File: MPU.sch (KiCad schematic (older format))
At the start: 32 parts, among them J1 MICRO-USB, P1 BL_PAD, P10 CONN_01X01, P11 CONN_01X04, P2 SWD_DAT, P3 SWD_CLK, P4 SWD_3V3, P5 SWD_GND, P6 SWD_RST, P8 CONN_01X01, P9 CONN_01X01, SW1 SW_PUSH, SW2 SW_PUSH, U4 SAMD21E17A, Y1 32.768kHz

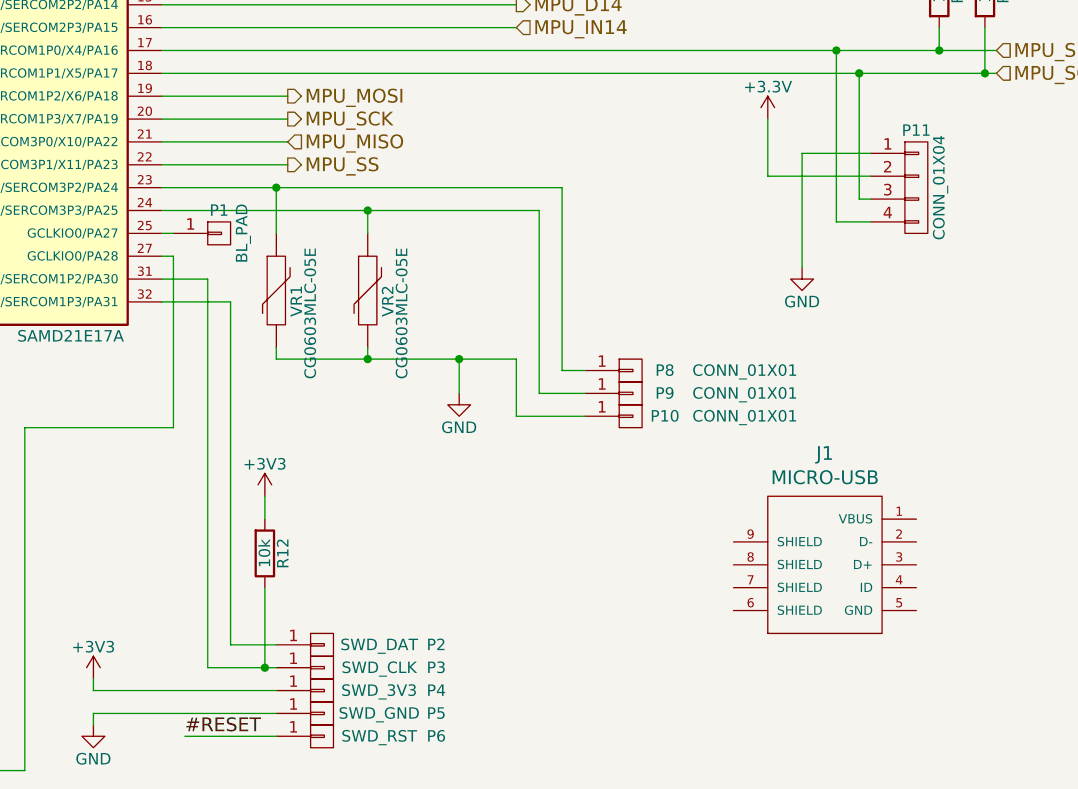
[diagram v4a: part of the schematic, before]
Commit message: Started work to add the power mux and USB connector
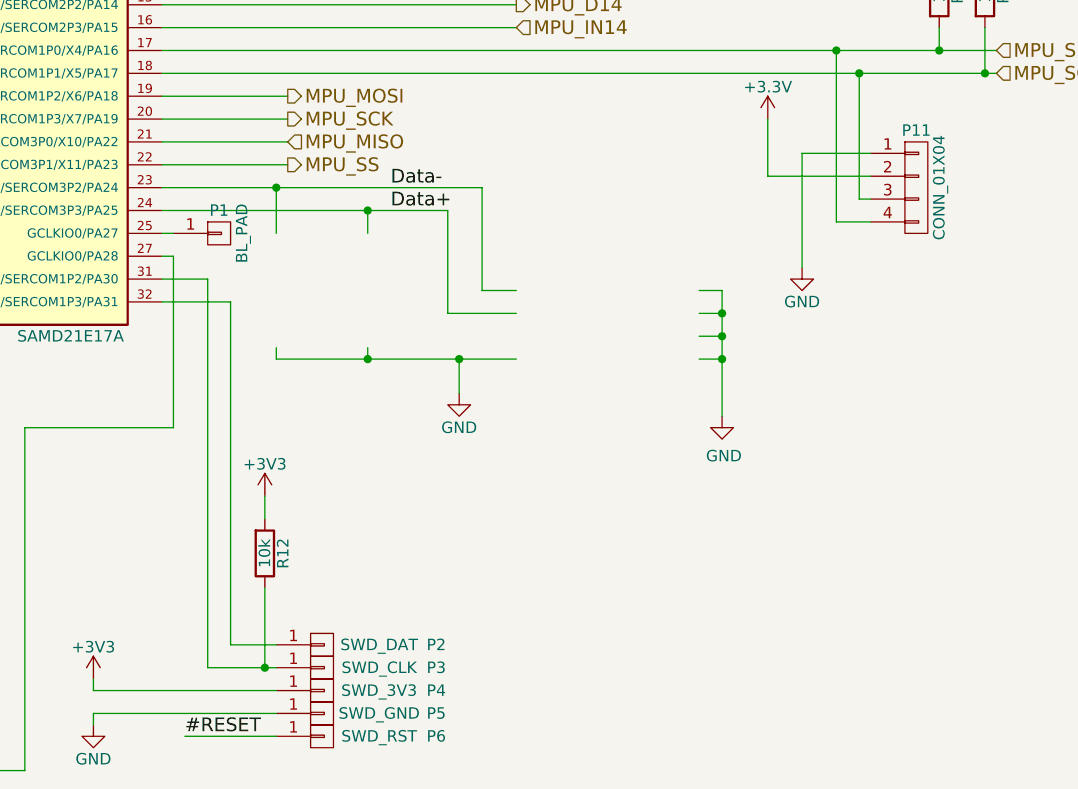
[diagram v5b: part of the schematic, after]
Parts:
- removed J1: MICRO-USB, RocketScreamKicadLibrary:MICRO-USB, symbol MICRO-USB
- removed P10, P8, P9: CONN_01X01, Measurement_Points:Measurement_Point_Round-TH_Small, symbol CONN_01X01
- removed VR1, VR2: CG0603MLC-05E, Capacitors_SMD:C_0603, symbol VR
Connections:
- net labels added: Data+, Data-
- wire segments 107 -> 110
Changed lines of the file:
@@
-	1    0    0    -1
-$EndComp
-$Comp
-L VR VR1
-U 1 1 56C25FED
-P 6150 4100
-F 0 "VR1" V 6210 4054 50  0000 C TNN
-F 1 "CG0603MLC-05E" V 6300 4000 50  0000 C CNN
-F 2 "Capacitors_SMD:C_0603" H 6150 4100 50  0001 C CNN
-F 3 "" H 6150 4100 50  0000 C CNN
-	1    6150 4100
-	1    0    0    -1
-$EndComp
-$Comp
-L VR VR2
-U 1 1 56C2603F
-P 6550 4100
-F 0 "VR2" V 6610 4054 50  0000 C TNN
-F 1 "CG0603MLC-05E" V 6700 4000 50  0000 C CNN
-F 2 "Capacitors_SMD:C_0603" H 6550 4100 50  0001 C CNN
-F 3 "" H 6550 4100 50  0000 C CNN
-	1    6550 4100
 	1    0    0    -1
 $EndComp
@@
 	1    0    0    -1
 $EndComp
-$Comp
-L CONN_01X01 P8
-U 1 1 56C3BE2F
-P 7700 4450
-F 0 "P8" H 7850 4450 50  0000 C CNN
-F 1 "CONN_01X01" H 8200 4450 50  0000 C CNN
-F 2 "Measurement_Points:Measurement_Point_Round-TH_Small" H 7700 4450 50  0001 C CNN
-F 3 "" H 7700 4450 50  0000 C CNN
-	1    7700 4450
-	1    0    0    -1
-$EndComp
-$Comp
-L CONN_01X01 P9
-U 1 1 56C3BE98
-P 7700 4550
-F 0 "P9" H 7850 4550 50  0000 C CNN
-F 1 "CONN_01X01" H 8200 4550 50  0000 C CNN
-F 2 "Measurement_Points:Measurement_Point_Round-TH_Small" H 7700 4550 50  0001 C CNN
-F 3 "" H 7700 4550 50  0000 C CNN
-	1    7700 4550
-	1    0    0    -1
-$EndComp
-$Comp
-L CONN_01X01 P10
-U 1 1 56C3BF04
-P 7700 4650
-F 0 "P10" H 7850 4650 50  0000 C CNN
-F 1 "CONN_01X01" H 8200 4650 50  0000 C CNN
-F 2 "Measurement_Points:Measurement_Point_Round-TH_Small" H 7700 4650 50  0001 C CNN
-F 3 "" H 7700 4650 50  0000 C CNN
-	1    7700 4650
-	1    0    0    -1
-$EndComp
 Wire Wire Line
 	9250 2950 9250 3150
@@
 Wire Wire Line
 	6150 4400 7200 4400
-Wire Wire Line
-	7200 4400 7200 4650
-Wire Wire Line
-	7200 4650 7500 4650
-Wire Wire Line
-	5650 3750 7300 3750
-Wire Wire Line
-	7300 3750 7300 4550
-Wire Wire Line
-	7300 4550 7500 4550
-Wire Wire Line
-	5650 3650 7400 3650
-Wire Wire Line
-	7400 3650 7400 4450
-Wire Wire Line
-	7400 4450 7500 4450
 Text HLabel 6200 3250 2    60   Output ~ 0
 MPU_MOSI
@@
 	6100 5400 6100 5750
 Connection ~ 6100 5750
-$Comp
-L MICRO-USB J1
-U 1 1 5700ADCA
-P 8550 5300
-F 0 "J1" H 8550 5787 60  0000 C CNN
-F 1 "MICRO-USB" H 8550 5681 60  0000 C CNN
-F 2 "RocketScreamKicadLibrary:MICRO-USB" H 8550 4850 60  0001 C CNN
-F 3 "" H 8600 5500 60  0000 C CNN
-	1    8550 5300
-	1    0    0    -1
-$EndComp
+Wire Wire Line
+	8000 4400 8100 4400
+$Comp
+L GND #PWR032
+U 1 1 5700C2DD
+P 8100 4650
+F 0 "#PWR032" H 8100 4400 50  0001 C CNN
+F 1 "GND" H 8108 4476 50  0000 C CNN
+F 2 "" H 8100 4650 50  0000 C CNN
+F 3 "" H 8100 4650 50  0000 C CNN
+	1    8100 4650
+	1    0    0    -1
+$EndComp
+Wire Wire Line
+	8000 4300 8100 4300
+Wire Wire Line
+	8100 4100 8100 4650
+Connection ~ 8100 4400
+Wire Wire Line
+	8000 4200 8100 4200
+Connection ~ 8100 4300
+Wire Wire Line
+	8000 4100 8100 4100
+Connection ~ 8100 4200
+Wire Wire Line
+	5650 3650 7050 3650
+Wire Wire Line
+	7050 3650 7050 4100
+Wire Wire Line
+	7050 4100 7200 4100
+Wire Wire Line
+	7200 4200 6900 4200
+Wire Wire Line
+	6900 4200 6900 3750
+Wire Wire Line
+	6900 3750 5650 3750
+Text Label 6650 3650 0    60   ~ 0
+Data-
+Text Label 6650 3750 0    60   ~ 0
+Data+
 $EndSCHEMATC

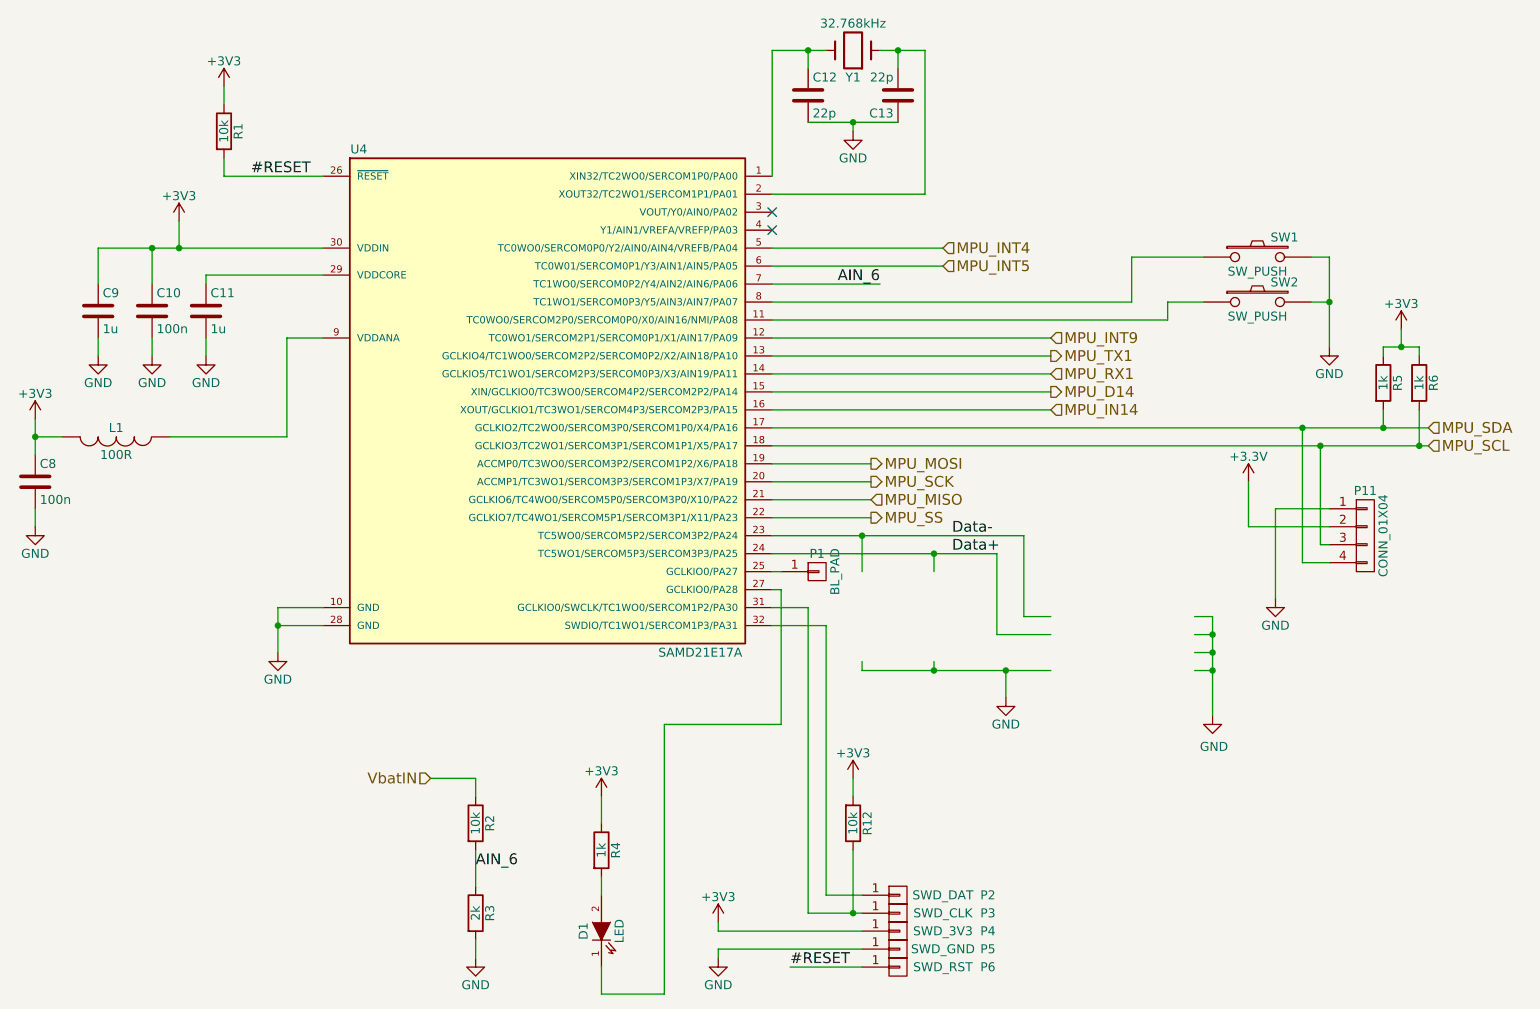
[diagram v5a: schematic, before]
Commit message: Added USB connector, diode or etc to layout@
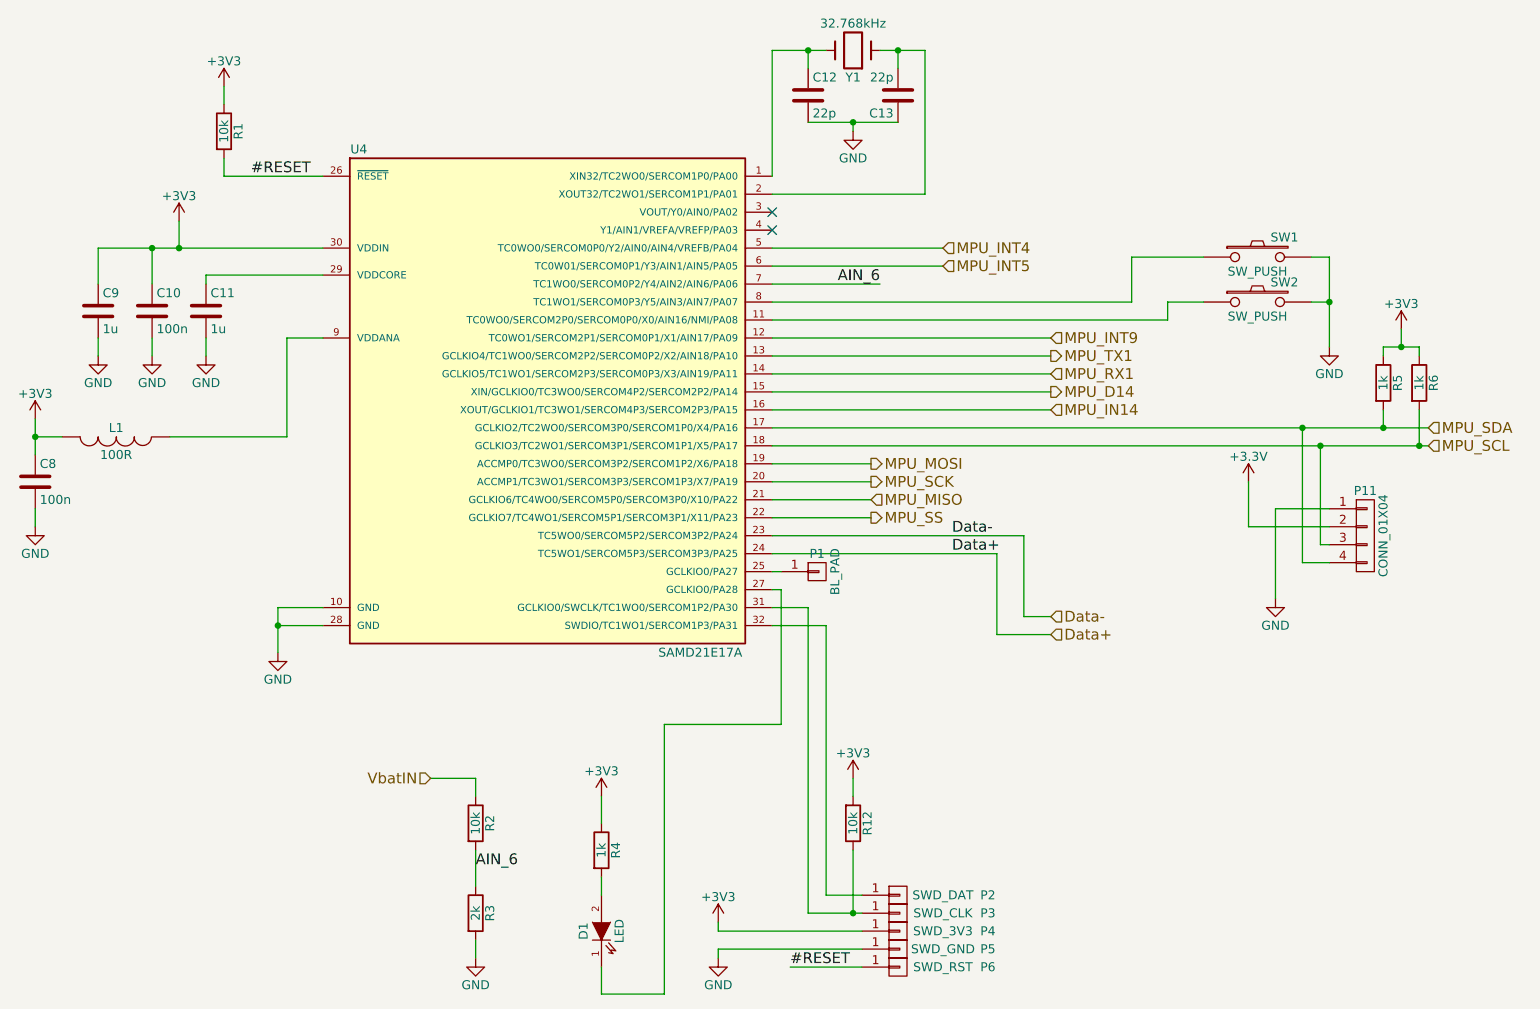
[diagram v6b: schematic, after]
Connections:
- wire segments 110 -> 99
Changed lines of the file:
@@
 	1    0    0    -1
 $EndComp
-$Comp
-L GND #PWR013
-U 1 1 56C13132
-P 6950 4550
-F 0 "#PWR013" H 6950 4300 50  0001 C CNN
-F 1 "GND" H 6950 4400 50  0000 C CNN
-F 2 "" H 6950 4550 50  0000 C CNN
-F 3 "" H 6950 4550 50  0000 C CNN
-	1    6950 4550
-	1    0    0    -1
-$EndComp
-Wire Wire Line
-	6950 4400 6950 4550
 Wire Wire Line
 	3150 2200 2500 2200
@@
 Connection ~ 2200 2050
 $Comp
-L GND #PWR014
+L GND #PWR013
 U 1 1 56C1336E
 P 1900 2650
-F 0 "#PWR014" H 1900 2400 50  0001 C CNN
+F 0 "#PWR013" H 1900 2400 50  0001 C CNN
 F 1 "GND" H 1900 2500 50  0000 C CNN
 F 2 "" H 1900 2650 50  0000 C CNN
@@
 $EndComp
 $Comp
-L GND #PWR015
+L GND #PWR014
 U 1 1 56C133A0
 P 2200 2650
-F 0 "#PWR015" H 2200 2400 50  0001 C CNN
+F 0 "#PWR014" H 2200 2400 50  0001 C CNN
 F 1 "GND" H 2200 2500 50  0000 C CNN
 F 2 "" H 2200 2650 50  0000 C CNN
@@
 $EndComp
 $Comp
-L GND #PWR016
+L GND #PWR015
 U 1 1 56C133D2
 P 2500 2650
-F 0 "#PWR016" H 2500 2400 50  0001 C CNN
+F 0 "#PWR015" H 2500 2400 50  0001 C CNN
 F 1 "GND" H 2500 2500 50  0000 C CNN
 F 2 "" H 2500 2650 50  0000 C CNN
@@
 $EndComp
 $Comp
-L +3V3 #PWR017
+L +3V3 #PWR016
 U 1 1 56C24D00
 P 9150 2500
-F 0 "#PWR017" H 9150 2350 50  0001 C CNN
+F 0 "#PWR016" H 9150 2350 50  0001 C CNN
 F 1 "+3V3" H 9150 2640 50  0000 C CNN
 F 2 "" H 9150 2500 50  0000 C CNN
@@
 	1    0    0    -1
 $EndComp
-Wire Wire Line
-	6150 3650 6150 3850
-Connection ~ 6150 3650
-Wire Wire Line
-	6550 3750 6550 3850
-Connection ~ 6550 3750
-Wire Wire Line
-	6550 4350 6550 4400
-Connection ~ 6950 4400
-Wire Wire Line
-	6150 4400 6150 4350
-Connection ~ 6550 4400
 $Comp
 L C C13
@@
 $EndComp
 $Comp
-L GND #PWR018
+L GND #PWR017
 U 1 1 56C269FF
 P 6100 1400
-F 0 "#PWR018" H 6100 1150 50  0001 C CNN
+F 0 "#PWR017" H 6100 1150 50  0001 C CNN
 F 1 "GND" H 6100 1250 50  0000 C CNN
 F 2 "" H 6100 1400 50  0000 C CNN
@@
 AIN_6
 $Comp
-L GND #PWR019
+L GND #PWR018
 U 1 1 56C278AB
 P 4000 6000
-F 0 "#PWR019" H 4000 5750 50  0001 C CNN
+F 0 "#PWR018" H 4000 5750 50  0001 C CNN
 F 1 "GND" H 4000 5850 50  0000 C CNN
 F 2 "" H 4000 6000 50  0000 C CNN
@@
 	1550 3000 1550 3200
 $Comp
-L GND #PWR020
+L GND #PWR019
 U 1 1 56C282F2
 P 1550 3600
-F 0 "#PWR020" H 1550 3350 50  0001 C CNN
+F 0 "#PWR019" H 1550 3350 50  0001 C CNN
 F 1 "GND" H 1550 3450 50  0000 C CNN
 F 2 "" H 1550 3600 50  0000 C CNN
@@
 	1550 3500 1550 3600
 $Comp
-L +3V3 #PWR021
+L +3V3 #PWR020
 U 1 1 56C28419
 P 1550 3000
-F 0 "#PWR021" H 1550 2850 50  0001 C CNN
+F 0 "#PWR020" H 1550 2850 50  0001 C CNN
 F 1 "+3V3" H 1550 3140 50  0000 C CNN
 F 2 "" H 1550 3000 50  0000 C CNN
@@
 	2600 1650 2600 1550
 $Comp
-L +3V3 #PWR022
+L +3V3 #PWR021
 U 1 1 56C28F33
 P 2600 1150
-F 0 "#PWR022" H 2600 1000 50  0001 C CNN
+F 0 "#PWR021" H 2600 1000 50  0001 C CNN
 F 1 "+3V3" H 2600 1290 50  0000 C CNN
 F 2 "" H 2600 1150 50  0000 C CNN
@@
 	2600 1150 2600 1250
 $Comp
-L +3V3 #PWR023
+L +3V3 #PWR022
 U 1 1 56C2B080
 P 5350 5800
-F 0 "#PWR023" H 5350 5650 50  0001 C CNN
+F 0 "#PWR022" H 5350 5650 50  0001 C CNN
 F 1 "+3V3" H 5350 5940 50  0000 C CNN
 F 2 "" H 5350 5800 50  0000 C CNN
@@
 $EndComp
 $Comp
-L GND #PWR024
+L GND #PWR023
 U 1 1 56C2B0D0
 P 5350 6000
-F 0 "#PWR024" H 5350 5750 50  0001 C CNN
+F 0 "#PWR023" H 5350 5750 50  0001 C CNN
 F 1 "GND" H 5350 5850 50  0000 C CNN
 F 2 "" H 5350 6000 50  0000 C CNN
@@
 	5350 5950 6150 5950
 $Comp
-L +3V3 #PWR025
+L +3V3 #PWR024
 U 1 1 56C2B3B6
 P 2350 1900
-F 0 "#PWR025" H 2350 1750 50  0001 C CNN
+F 0 "#PWR024" H 2350 1750 50  0001 C CNN
 F 1 "+3V3" H 2350 2040 50  0000 C CNN
 F 2 "" H 2350 1900 50  0000 C CNN
@@
 Connection ~ 2350 2050
 $Comp
-L GND #PWR026
+L GND #PWR025
 U 1 1 56C39EB2
 P 2900 4300
-F 0 "#PWR026" H 2900 4050 50  0001 C CNN
+F 0 "#PWR025" H 2900 4050 50  0001 C CNN
 F 1 "GND" H 2900 4150 50  0000 C CNN
 F 2 "" H 2900 4300 50  0000 C CNN
@@
 	4700 6200 4700 6050
 $Comp
-L +3V3 #PWR027
+L +3V3 #PWR026
 U 1 1 56C3A13C
 P 4700 5100
-F 0 "#PWR027" H 4700 4950 50  0001 C CNN
+F 0 "#PWR026" H 4700 4950 50  0001 C CNN
 F 1 "+3V3" H 4700 5240 50  0000 C CNN
 F 2 "" H 4700 5100 50  0000 C CNN
@@
 $EndComp
 Wire Wire Line
-	9250 2950 9250 3150
+	9250 3150 9250 2950
 Connection ~ 9250 3150
 $Comp
@@
 Connection ~ 6100 1350
 Wire Wire Line
-	5950 950  5650 950
+	5650 950  5950 950
 Wire Wire Line
 	5650 950  5650 1650
@@
 $EndComp
 Wire Wire Line
-	9300 3050 5650 3050
+	5650 3050 9300 3050
 Wire Wire Line
 	5650 3150 9300 3150
-Wire Wire Line
-	6150 4400 7200 4400
 Text HLabel 6200 3250 2    60   Output ~ 0
 MPU_MOSI
@@
 $EndComp
 $Comp
-L GND #PWR028
+L GND #PWR027
 U 1 1 56EAE5DD
 P 8450 4000
-F 0 "#PWR028" H 8450 3750 50  0001 C CNN
+F 0 "#PWR027" H 8450 3750 50  0001 C CNN
 F 1 "GND" H 8450 3850 50  0000 C CNN
 F 2 "" H 8450 4000 50  0000 C CNN
@@
 $EndComp
 $Comp
-L +3.3V #PWR029
+L +3.3V #PWR028
 U 1 1 56EAE62B
 P 8300 3350
-F 0 "#PWR029" H 8300 3200 50  0001 C CNN
+F 0 "#PWR028" H 8300 3200 50  0001 C CNN
 F 1 "+3.3V" H 8300 3490 50  0000 C CNN
 F 2 "" H 8300 3350 50  0000 C CNN
@@
 $EndComp
 $Comp
-L GND #PWR030
+L GND #PWR029
 U 1 1 56EC2766
 P 8750 2600
-F 0 "#PWR030" H 8750 2350 50  0001 C CNN
+F 0 "#PWR029" H 8750 2350 50  0001 C CNN
 F 1 "GND" H 8750 2450 50  0000 C CNN
 F 2 "" H 8750 2600 50  0000 C CNN
@@
 $EndComp
 $Comp
-L +3V3 #PWR031
+L +3V3 #PWR030
 U 1 1 56F90C8F
 P 6100 5000
-F 0 "#PWR031" H 6100 4850 50  0001 C CNN
+F 0 "#PWR030" H 6100 4850 50  0001 C CNN
 F 1 "+3V3" H 6100 5140 50  0000 C CNN
 F 2 "" H 6100 5000 50  0000 C CNN
@@
 	6100 5400 6100 5750
 Connection ~ 6100 5750
-Wire Wire Line
-	8000 4400 8100 4400
-$Comp
-L GND #PWR032
-U 1 1 5700C2DD
-P 8100 4650
-F 0 "#PWR032" H 8100 4400 50  0001 C CNN
-F 1 "GND" H 8108 4476 50  0000 C CNN
-F 2 "" H 8100 4650 50  0000 C CNN
-F 3 "" H 8100 4650 50  0000 C CNN
-	1    8100 4650
-	1    0    0    -1
-$EndComp
-Wire Wire Line
-	8000 4300 8100 4300
-Wire Wire Line
-	8100 4100 8100 4650
-Connection ~ 8100 4400
-Wire Wire Line
-	8000 4200 8100 4200
-Connection ~ 8100 4300
-Wire Wire Line
-	8000 4100 8100 4100
-Connection ~ 8100 4200
 Wire Wire Line
 	5650 3650 7050 3650
@@
 Text Label 6650 3750 0    60   ~ 0
 Data+
+Text HLabel 7200 4100 2    60   Input ~ 0
+Data-
+Text HLabel 7200 4200 2    60   Input ~ 0
+Data+
 $EndSCHEMATC
